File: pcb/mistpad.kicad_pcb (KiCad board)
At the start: 2 copper layers, 61.7 x 54.5 mm, 11 parts, among them J1 OLED_DISP, SW1 SW_Push, SW2 SW_Push, SW3 SW_Push, SW4 SW_Push, U1 XIAO-RP2040-DIP

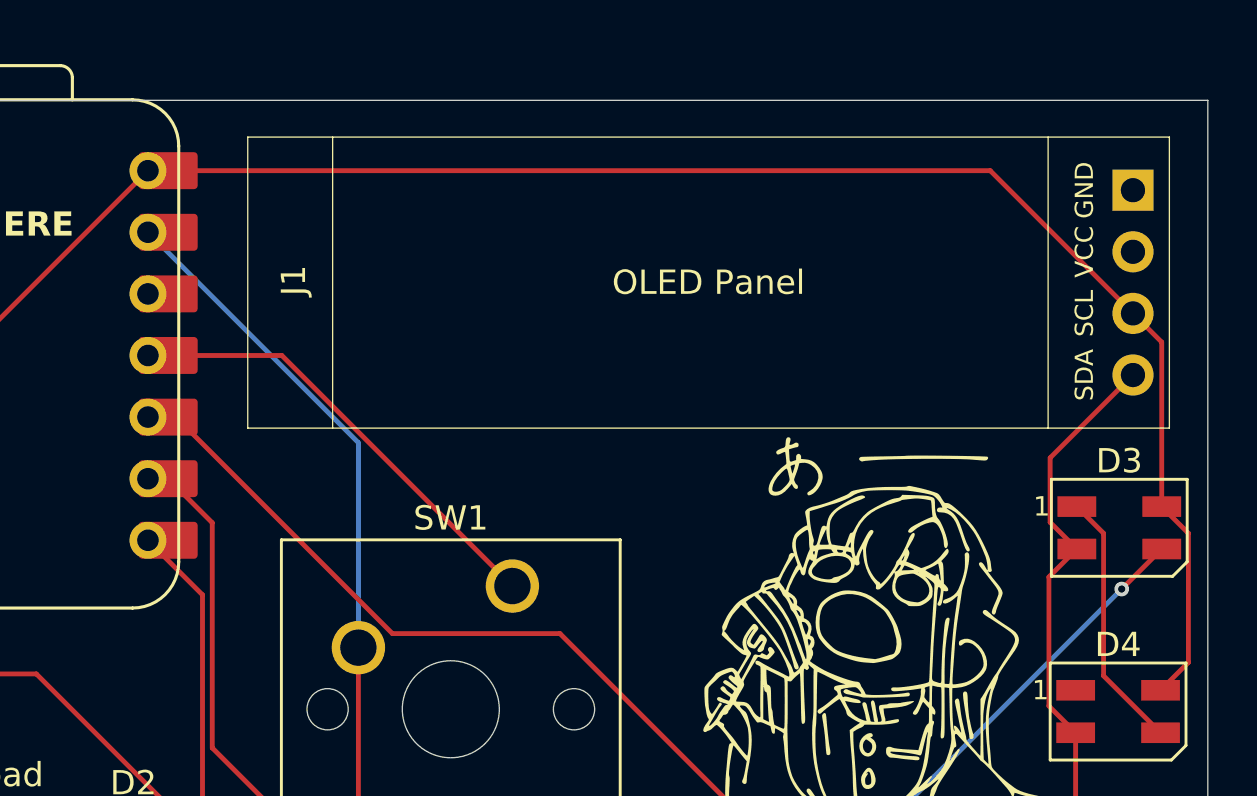
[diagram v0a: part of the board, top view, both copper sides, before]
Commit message: Modified PCB (display orientation)
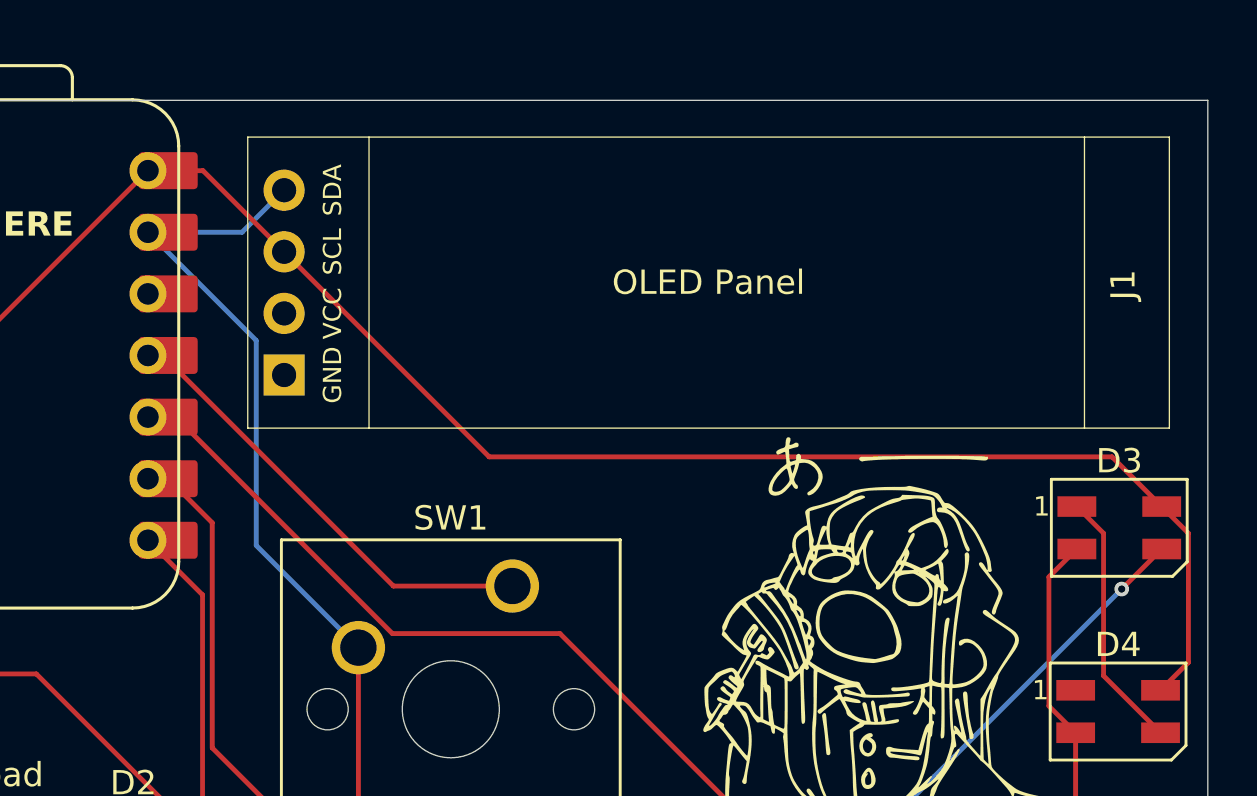
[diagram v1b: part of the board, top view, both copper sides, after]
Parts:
- moved J1 39.8 mm to (158.2, 76.5), turned to 180 degrees
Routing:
- net +5V: track 101.9 -> 97.9 mm
- net GND: track 148.4 -> 145.7 mm
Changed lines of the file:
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@@
 	(footprint "OLED Lib:SSD1306-0.91-OLED-4pin-128x32"
 		(layer "F.Cu")
-		(at 120.215 64.515)
+		(at 158.215 76.515 180)
 		(property "Reference" "J1"
 			(at 1.9 5.91 90)
@@
 		(attr through_hole)
 		(fp_line
+			(start 38 12)
+			(end 38 0)
+			(stroke
+				(width 0.04)
+				(type solid)
+			)
+			(layer "F.SilkS")
+		)
+		(fp_line
+			(start 38 0)
+			(end 0 0)
+			(stroke
+				(width 0.04)
+				(type solid)
+			)
+			(layer "F.SilkS")
+		)
+		(fp_line
+			(start 33 0)
+			(end 33 12)
+			(stroke
+				(width 0.04)
+				(type solid)
+			)
+			(layer "F.SilkS")
+		)
+		(fp_line
+			(start 3.5 0)
+			(end 3.5 12)
+			(stroke
+				(width 0.04)
+				(type solid)
+			)
+			(layer "F.SilkS")
+		)
+		(fp_line
+			(start 0 12)
+			(end 38 12)
+			(stroke
+				(width 0.04)
+				(type solid)
+			)
+			(layer "F.SilkS")
+		)
+		(fp_line
 			(start 0 0)
 			(end 0 12)
@@
 		)
 		(fp_line
+			(start 38 12)
+			(end 38 0)
+			(stroke
+				(width 0.04)
+				(type solid)
+			)
+			(layer "F.CrtYd")
+		)
+		(fp_line
+			(start 38 0)
+			(end 0 0)
+			(stroke
+				(width 0.04)
+				(type solid)
+			)
+			(layer "F.CrtYd")
+		)
+		(fp_line
 			(start 0 12)
 			(end 38 12)
@@
 				(type solid)
 			)
-			(layer "F.SilkS")
-		)
-		(fp_line
-			(start 3.5 0)
-			(end 3.5 12)
-			(stroke
-				(width 0.04)
-				(type solid)
-			)
-			(layer "F.SilkS")
-		)
-		(fp_line
-			(start 33 0)
-			(end 33 12)
-			(stroke
-				(width 0.04)
-				(type solid)
-			)
-			(layer "F.SilkS")
-		)
-		(fp_line
-			(start 38 0)
-			(end 0 0)
-			(stroke
-				(width 0.04)
-				(type solid)
-			)
-			(layer "F.SilkS")
-		)
-		(fp_line
-			(start 38 12)
-			(end 38 0)
-			(stroke
-				(width 0.04)
-				(type solid)
-			)
-			(layer "F.SilkS")
+			(layer "F.CrtYd")
 		)
 		(fp_line
@@
 			(layer "F.CrtYd")
 		)
-		(fp_line
-			(start 0 12)
-			(end 38 12)
-			(stroke
-				(width 0.04)
-				(type solid)
-			)
-			(layer "F.CrtYd")
-		)
-		(fp_line
-			(start 38 0)
-			(end 0 0)
-			(stroke
-				(width 0.04)
-				(type solid)
-			)
-			(layer "F.CrtYd")
-		)
-		(fp_line
-			(start 38 12)
-			(end 38 0)
-			(stroke
-				(width 0.04)
-				(type solid)
-			)
-			(layer "F.CrtYd")
-		)
 		(fp_text user "OLED Panel"
 			(at 19 6 0)
@@
 		)
 		(fp_text user "VCC"
-			(at 34.5 4.73 270)
+			(at 34.5 4.73 90)
 			(layer "F.SilkS")
 			(effects
@@
 		)
 		(fp_text user "GND"
-			(at 34.5 2.19 270)
+			(at 34.5 2.19 90)
 			(layer "F.SilkS")
 			(effects
@@
 		)
 		(fp_text user "SDA"
-			(at 34.5 9.81 270)
+			(at 34.5 9.81 90)
 			(layer "F.SilkS")
 			(effects
@@
 		)
 		(fp_text user "SCL"
-			(at 34.5 7.27 270)
+			(at 34.5 7.27 90)
 			(layer "F.SilkS")
 			(effects
@@
 		)
 		(pad "1" thru_hole rect
-			(at 36.5 2.19)
+			(at 36.5 2.19 180)
 			(size 1.7 1.7)
 			(drill 1)
@@
 		)
 		(pad "2" thru_hole oval
-			(at 36.5 4.73)
+			(at 36.5 4.73 180)
 			(size 1.7 1.7)
 			(drill 1)
@@
 		)
 		(pad "3" thru_hole oval
-			(at 36.5 7.27)
+			(at 36.5 7.27 180)
 			(size 1.7 1.7)
 			(drill 1)
@@
 		)
 		(pad "4" thru_hole oval
-			(at 36.5 9.81)
+			(at 36.5 9.81 180)
 			(size 1.7 1.7)
 			(drill 1)
@@
 	)
 	(segment
-		(start 150.83 65.9)
+		(start 118.37 65.9)
 		(end 116.1 65.9)
 		(width 0.2)
@@
 	)
 	(segment
-		(start 157.9 72.97)
-		(end 156.715 71.785)
-		(width 0.2)
-		(layer "F.Cu")
-		(net 1)
-	)
-	(segment
 		(start 159.001 80.851)
 		(end 157.9 79.75)
@@
 	)
 	(segment
-		(start 157.9 79.75)
-		(end 157.9 72.97)
-		(width 0.2)
-		(layer "F.Cu")
-		(net 1)
-	)
-	(segment
 		(start 157.85 87.325)
 		(end 159.001 86.174)
@@
 	)
 	(segment
+		(start 155.85 77.7)
+		(end 130.17 77.7)
+		(width 0.2)
+		(layer "F.Cu")
+		(net 1)
+	)
+	(segment
 		(start 117.25 93.025)
 		(end 117.25 92.4)
@@
 	)
 	(segment
-		(start 156.715 71.785)
-		(end 150.83 65.9)
+		(start 121.715 69.245)
+		(end 118.37 65.9)
 		(width 0.2)
 		(layer "F.Cu")
@@
 	)
 	(segment
+		(start 130.17 77.7)
+		(end 121.715 69.245)
+		(width 0.2)
+		(layer "F.Cu")
+		(net 1)
+	)
+	(segment
+		(start 157.9 79.75)
+		(end 155.85 77.7)
+		(width 0.2)
+		(layer "F.Cu")
+		(net 1)
+	)
+	(segment
 		(start 103 78.2)
 		(end 100.86 76.06)
@@
 	)
 	(segment
-		(start 153.299 80.399)
-		(end 153.299 77.741)
-		(width 0.2)
-		(layer "F.Cu")
-		(net 4)
-	)
-	(segment
-		(start 153.299 77.741)
-		(end 156.715 74.325)
-		(width 0.2)
-		(layer "F.Cu")
-		(net 4)
-	)
-	(segment
 		(start 105.7275 96.0225)
 		(end 106.975 94.775)
@@
 	)
 	(segment
-		(start 154.4 81.5)
-		(end 153.299 80.399)
-		(width 0.2)
-		(layer "F.Cu")
-		(net 4)
-	)
-	(segment
 		(start 113.75 94.775)
 		(end 106.975 94.775)
@@
 	)
 	(segment
-		(start 124.7775 77.1175)
+		(start 121.715 66.705)
+		(end 119.98 68.44)
+		(width 0.2)
+		(layer "B.Cu")
+		(net 4)
+	)
+	(segment
+		(start 124.7775 85.56625)
+		(end 120.564 81.35275)
+		(width 0.2)
+		(layer "B.Cu")
+		(net 4)
+	)
+	(segment
+		(start 120.564 81.35275)
+		(end 120.564 72.904)
+		(width 0.2)
+		(layer "B.Cu")
+		(net 4)
+	)
+	(segment
+		(start 120.564 72.904)
 		(end 116.1 68.44)
 		(width 0.2)
@@
 	)
 	(segment
-		(start 124.7775 85.56625)
-		(end 124.7775 77.1175)
+		(start 119.98 68.44)
+		(end 116.1 68.44)
 		(width 0.2)
 		(layer "B.Cu")
@@
 	)
 	(segment
+		(start 116.713626 73.52)
+		(end 116.1 73.52)
+		(width 0.2)
+		(layer "F.Cu")
+		(net 8)
+	)
+	(segment
+		(start 126.219876 83.02625)
+		(end 116.713626 73.52)
+		(width 0.2)
+		(layer "F.Cu")
+		(net 8)
+	)
+	(segment
 		(start 131.1275 83.02625)
-		(end 121.62125 73.52)
-		(width 0.2)
-		(layer "F.Cu")
-		(net 8)
-	)
-	(segment
-		(start 121.62125 73.52)
-		(end 116.1 73.52)
-		(width 0.2)
-		(layer "F.Cu")
+		(end 126.219876 83.02625)
+		(width 0.2)
+		(layer "F.Cu")
